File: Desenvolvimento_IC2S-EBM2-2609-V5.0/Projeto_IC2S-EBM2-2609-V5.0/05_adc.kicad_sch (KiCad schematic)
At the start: 6 parts, among them U7 MCP3208T-BI/SL

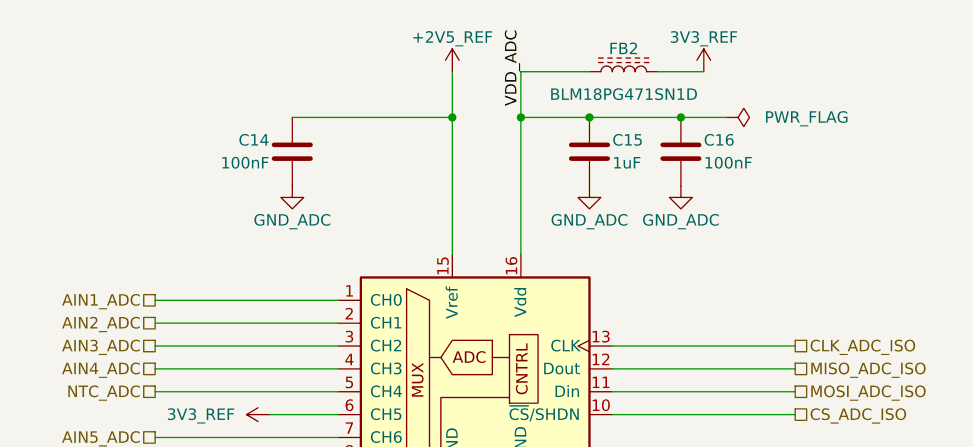
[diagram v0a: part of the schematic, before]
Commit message: Revisao de 28-09 (vinda da EBM7): ramo unico de 24 V, 100 nF a 50 V, um so MPN de 1 uF
- Saem F1 (250 mA), D3 e R3: o F1 nao aguenta o arranque da placa toda e o R3
  so existia para o limitar. F2 + D4 alimentam o U1 e os lacos; +24V_REG passa
  a +24V_ADC. C1 fica (Cin do TPS7A4001). Esquematico e PCB (sem pistas).
- 100 nF fora do 24 V -> TDK C1608X7R1H104K080AA (50 V); C29 (+24V_ADC) fica
  GRM188R72A104KA35D (100 V). 1 uF -> TDK C1608X7R1H105K080AB.
- Folha 2 notas 3, 11, 13 e 14; BOM preliminar regenerada; README, registo e
  lista de datasheets. Alteracao posterior ao Portao 1, registada como tal.

Co-Authored-By: Claude Opus 5.5 (1M context) <noreply@anthropic.com>
Claude-Session: https://claude.ai/code/session_01KPnkiJQKrkjgRqqw9M78ie
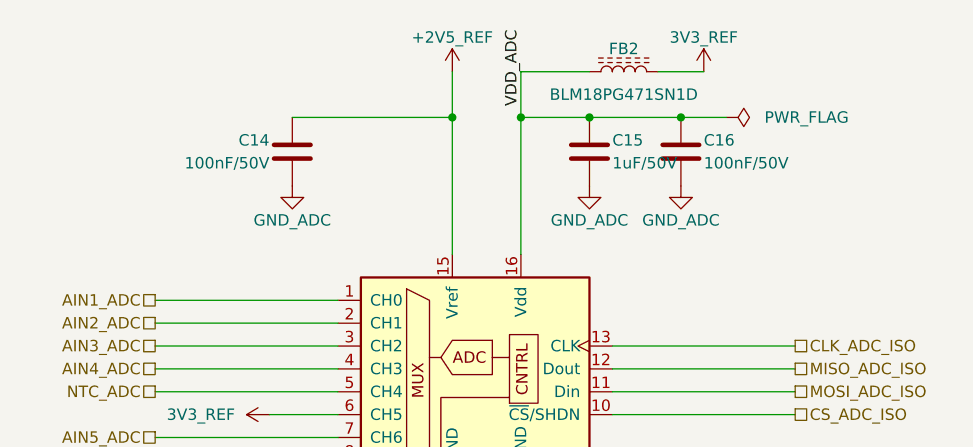
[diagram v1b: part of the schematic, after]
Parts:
- C14, C16: value 100nF -> 100nF/50V; MPN GRM188R72A104KA35D -> C1608X7R1H104K080AA
- C15: value 1uF -> 1uF/50V; MPN C0603C105K4RACTU -> C1608X7R1H105K080AB
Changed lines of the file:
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@@
 			)
 		)
-		(property "Value" "100nF"
+		(property "Value" "100nF/50V"
 			(at 116.84 68.58 0)
 			(show_name no)
@@
 			)
 		)
-		(property "MPN" "GRM188R72A104KA35D"
+		(property "MPN" "C1608X7R1H104K080AA"
 			(at 119.38 67.31 0)
 			(hide yes)
@@
 			)
 		)
-		(property "Value" "1uF"
+		(property "Value" "1uF/50V"
 			(at 154.94 68.58 0)
 			(show_name no)
@@
 			)
 		)
-		(property "MPN" "C0603C105K4RACTU"
+		(property "MPN" "C1608X7R1H105K080AB"
 			(at 152.4 67.31 0)
 			(hide yes)
@@
 			)
 		)
-		(property "Value" "100nF"
+		(property "Value" "100nF/50V"
 			(at 165.1 68.58 0)
 			(show_name no)
@@
 			)
 		)
-		(property "MPN" "GRM188R72A104KA35D"
+		(property "MPN" "C1608X7R1H104K080AA"
 			(at 162.56 67.31 0)
 			(hide yes)
